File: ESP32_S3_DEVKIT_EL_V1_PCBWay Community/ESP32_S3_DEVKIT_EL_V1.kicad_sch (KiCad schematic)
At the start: 84 parts, among them J1 12,15,17,18,19,20,21,22, J10 BUTTONS, J11 3v3, J12 RJ25, J13 RJ25, J14 RJ25, J15 12,15,17,18,19,20,21,22, J22 GPIO, J23 GPIO2, J3 LEDS, J30 GND, J31 5v, J32 Conn_01x03_Pin, J33 GND, J4 4,5,6,7,8,9,10,11, J5 23,24,25,31, J7 4,5,6,7,8,9,10,11, J9 ANSEL, U4 RA-02

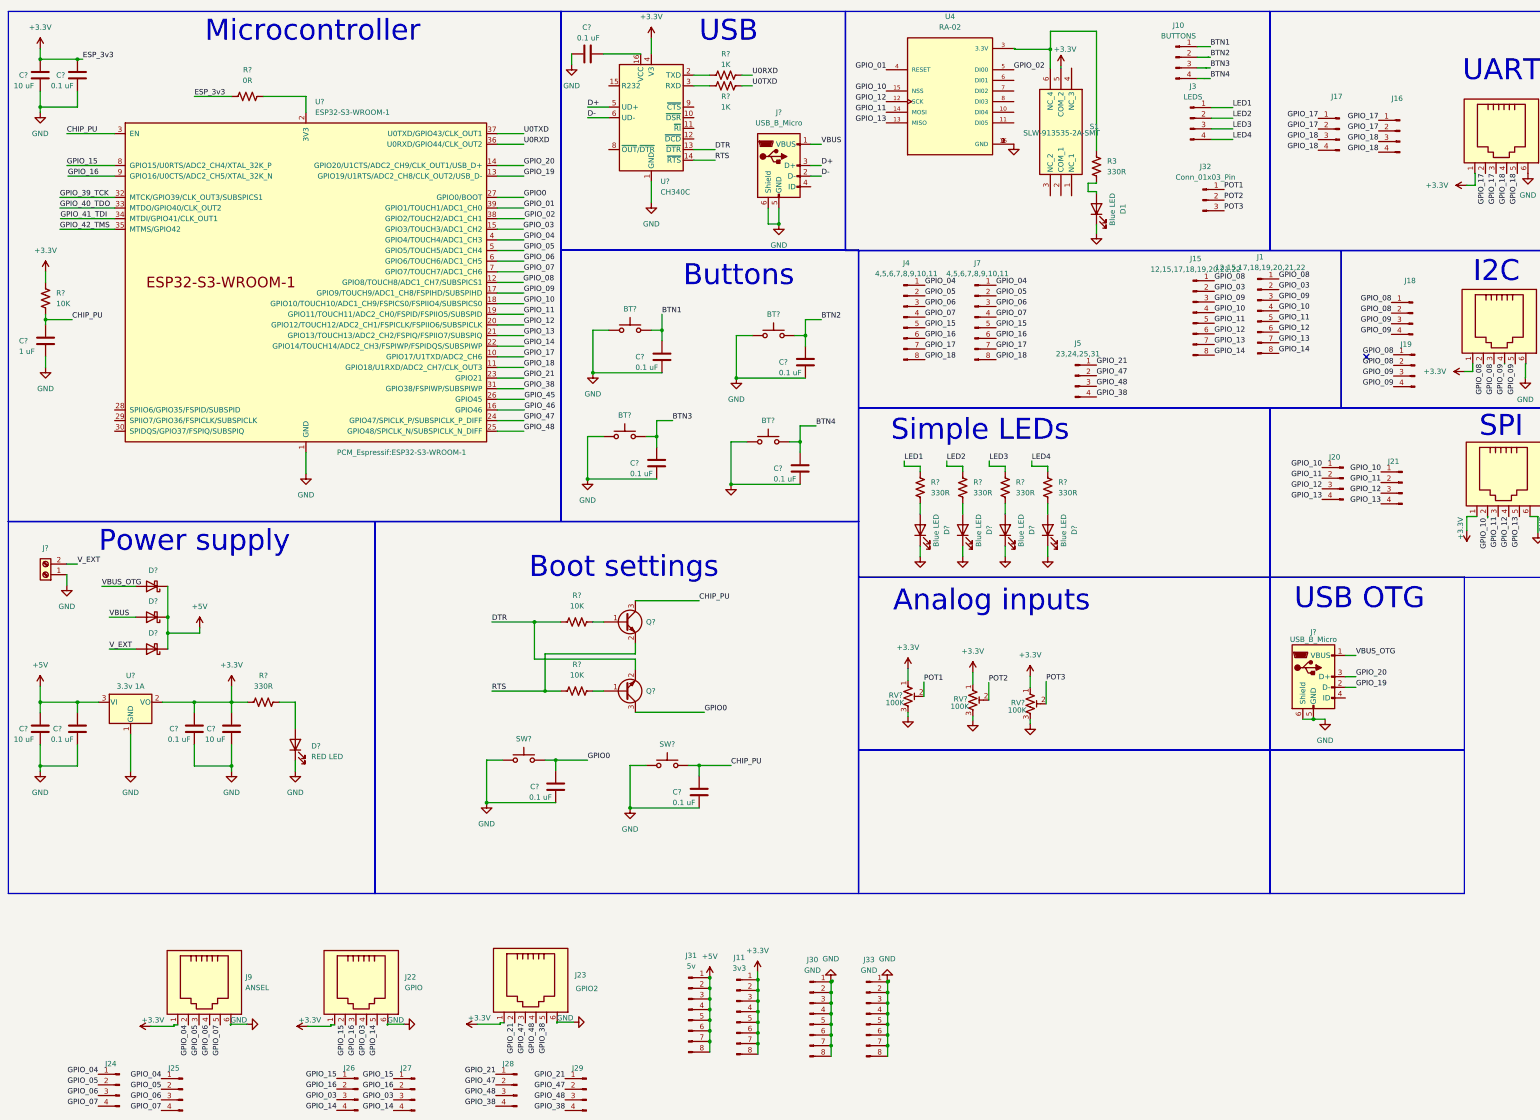
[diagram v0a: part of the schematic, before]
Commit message: Nueva version del esquematico de la placa
La unica modificacion que hice fue organizar un poco mejor el esquematico, osea el archivo .kicad_sch
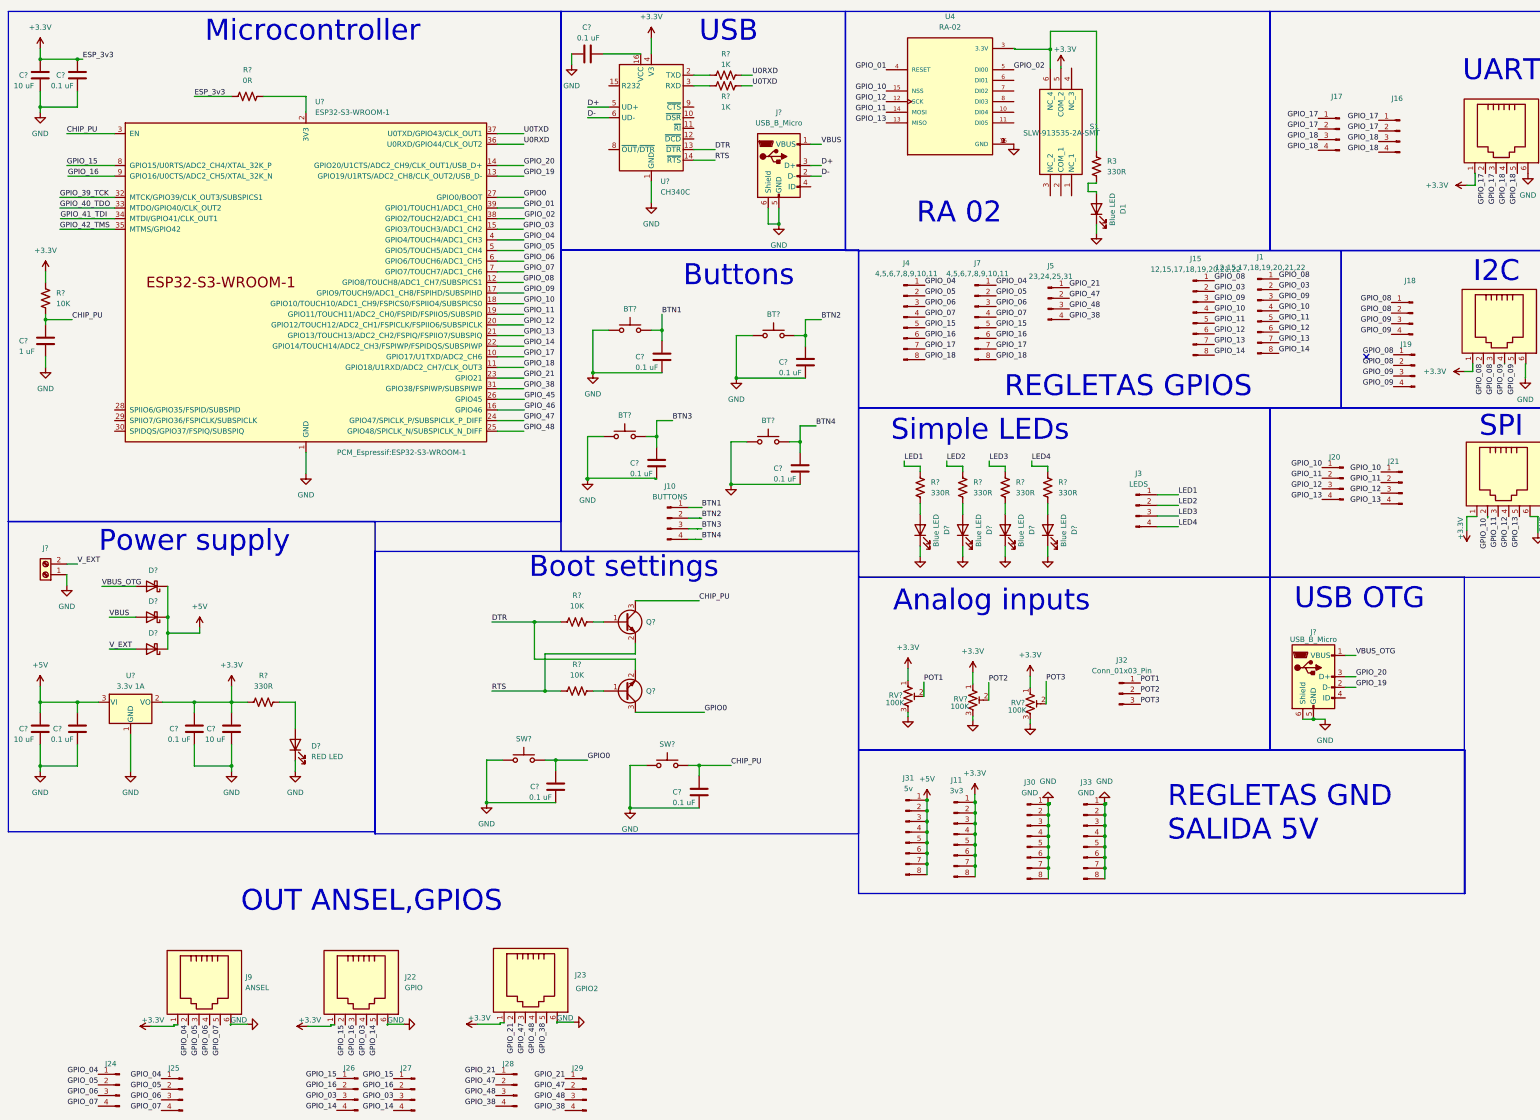
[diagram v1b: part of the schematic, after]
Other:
- note added: "OUT ANSEL,GPIOS"
- note added: "RA 02"
- note added: "REGLETAS GND SALIDA 5V"
- note added: "REGLETAS GPIOS"
- moved on the sheet: J10, J11, J3, J30, J31, J32, J33, J5
